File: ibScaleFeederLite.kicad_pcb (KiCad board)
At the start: 4 copper layers, 51.6 x 89 mm, 88 parts, among them J1 PEEL, J2 DRIVE, J3 RAIL, J4 SWD, J5 Serial, SW1 DOWN, SW2 UP, SW3 BOOT, U2 DRV8837, U3 DRV8837, U4 THVD1400D, U5 TPS563300, U6 AMS1117-3.3, U9 STM32F031C6Tx, Y1 8MHz

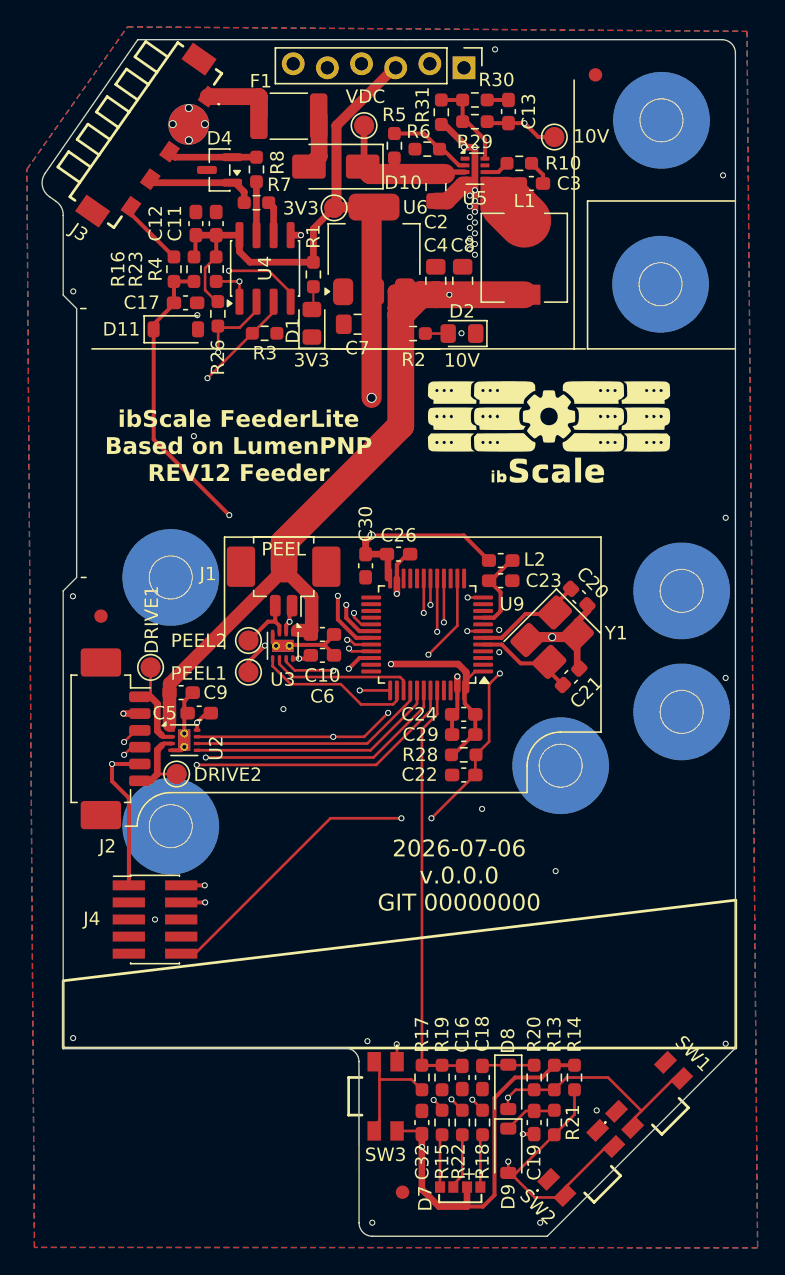
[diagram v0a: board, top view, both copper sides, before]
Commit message: Add labeling to SWD connector
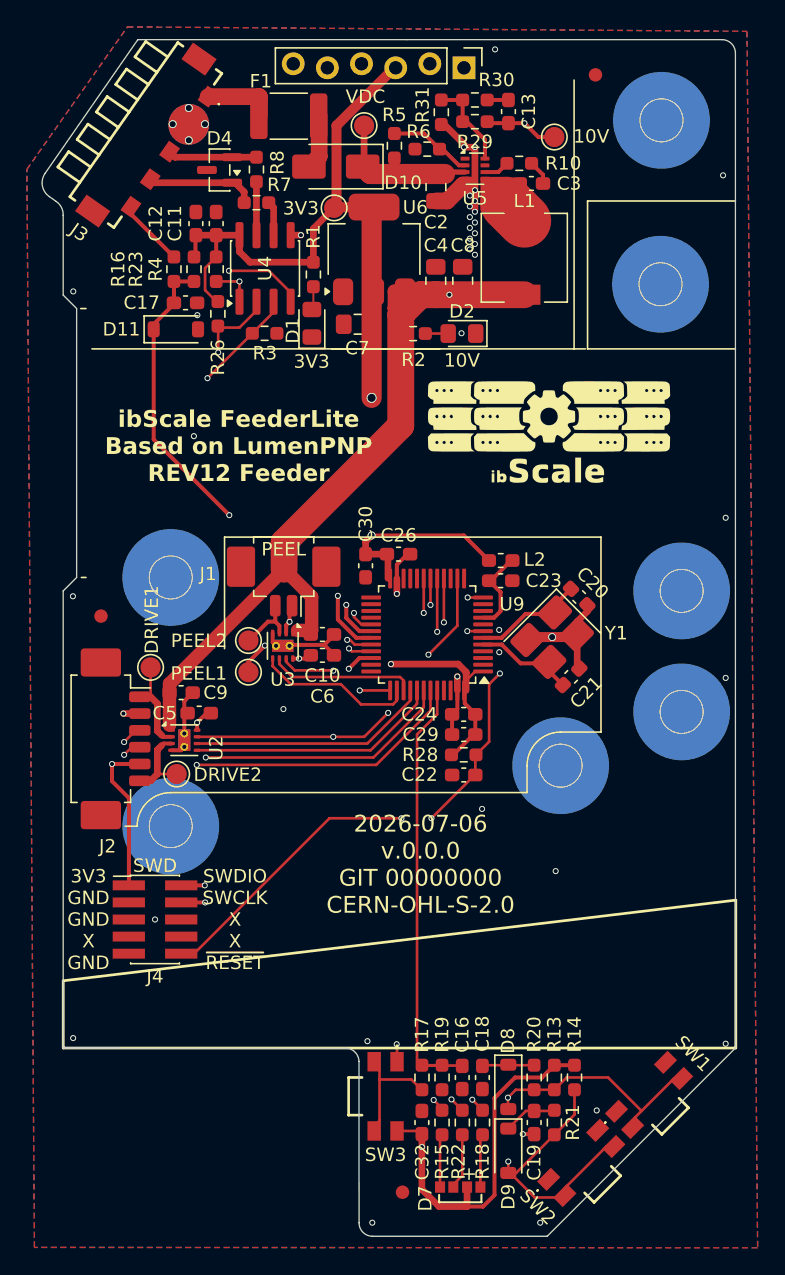
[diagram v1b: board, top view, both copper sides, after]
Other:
- board text added: "2026-07-06 v.0.0.0 GIT 00000000 CERN-OHL-S-2.0"
- board text added: "3V3 GND GND X GND"
- board text added: "SWDIO SWCLK X X ~{RESET}"
- board text removed: "2026-07-06 v.0.0.0 GIT 00000000"
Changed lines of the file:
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@@
 	)
 	(footprint "ibScale:PTCFVTR"
+		(locked yes)
 		(layer "F.Cu")
 		(at 120 104.55 -90)
@@
 	)
 	(footprint "ibScale:PTCFVTR"
+		(locked yes)
 		(layer "F.Cu")
 		(at 134.554594 109.504594 45)
@@
 	)
 	(footprint "ibScale:PTCFVTR"
+		(locked yes)
 		(layer "F.Cu")
 		(at 139.595406 104.445406 45)
@@
 		)
 		(property "Value" "3V3"
-			(at -2.747653 -0.018486 180)
+			(at -2.847653 -0.018486 180)
 			(layer "F.SilkS")
 			(effects
@@
 		(tags "Surface mounted pin header SMD 2x05 1.27mm double row")
 		(property "Reference" "J4"
-			(at -4.7 -0.05 0)
+			(at -0.001274 4.228619 0)
 			(layer "F.SilkS")
 			(effects
@@
 		)
 		(property "Value" "SWD"
-			(at 0 4.285 0)
-			(layer "F.Fab")
+			(at 0.000545 -4.005974 0)
+			(layer "F.SilkS")
 			(effects
 				(font
@@
 		(layer "Edge.Cuts")
 	)
+	(gr_text "3V3\nGND\nGND\nX\nGND"
+		(at 97.9 91.4 0)
+		(layer "F.SilkS")
+		(effects
+			(font
+				(size 1 1)
+				(thickness 0.15)
+			)
+		)
+	)
+	(gr_text "SWDIO\nSWCLK\nX\nX\n~{RESET}"
+		(at 108.8 91.4 0)
+		(layer "F.SilkS")
+		(effects
+			(font
+				(size 1 1)
+				(thickness 0.15)
+			)
+		)
+	)
 	(gr_text "PEEL"
 		(at 112.419869 63.857914 0)
@@
 		)
 	)
-	(gr_text "2026-07-06\nv.0.0.0\nGIT 00000000"
-		(at 125.476 88.138 0)
+	(gr_text "2026-07-06\nv.0.0.0\nGIT 00000000\nCERN-OHL-S-2.0"
+		(at 122.6 87.3 0)
 		(layer "F.SilkS")
 		(effects
@@
 	)
 	(segment
-		(start 122.7066 102.2375)
-		(end 122.7066 77.2634)
+		(start 122.338599 101.869499)
+		(end 122.338599 77.631401)
 		(width 0.2)
 		(layer "F.Cu")
@@
 	)
 	(segment
+		(start 123.8375 76.1325)
+		(end 123.8375 74.3625)
+		(width 0.2)
+		(layer "F.Cu")
+		(net "/BOOT0")
+	)
+	(segment
 		(start 125.61316 102.2625)
 		(end 125.66316 102.3125)
@@
 	)
 	(segment
-		(start 123.8375 76.1325)
-		(end 123.8375 74.3625)
+		(start 122.338599 77.631401)
+		(end 123.8375 76.1325)
 		(width 0.2)
 		(layer "F.Cu")
@@
 	)
 	(segment
-		(start 122.7066 77.2634)
-		(end 123.8375 76.1325)
+		(start 122.7066 102.2375)
+		(end 122.338599 101.869499)
 		(width 0.2)
 		(layer "F.Cu")
@@
 	)
 	(segment
-		(start 107.55 49.225)
-		(end 107.55 47.375)
+		(start 117.35 70.6)
+		(end 117.7 70.95)
 		(width 0.2)
 		(layer "F.Cu")
@@
 	)
 	(segment
-		(start 117.35 70.6)
-		(end 117.7 70.95)
+		(start 117.143955 70.6)
+		(end 117.35 70.6)
 		(width 0.2)
 		(layer "F.Cu")
@@
 	)
 	(segment
-		(start 109.15 47.375)
-		(end 110.4 46.125)
+		(start 107.55 49.225)
+		(end 107.55 47.375)
 		(width 0.2)
 		(layer "F.Cu")
@@
 	)
 	(segment
-		(start 117.143955 70.6)
-		(end 117.35 70.6)
+		(start 107.55 47.375)
+		(end 109.130618 47.375)
 		(width 0.2)
 		(layer "F.Cu")
@@
 	)
 	(segment
-		(start 107.55 47.375)
-		(end 109.15 47.375)
+		(start 117.7 70.95)
+		(end 118.925 70.95)
 		(width 0.2)
 		(layer "F.Cu")
@@
 	)
 	(segment
-		(start 110.4 46.125)
+		(start 110.4 46.105618)
 		(end 110.4 45.44837)
 		(width 0.2)
@@
 	)
 	(segment
-		(start 117.7 70.95)
-		(end 118.925 70.95)
+		(start 109.130618 47.375)
+		(end 110.4 46.105618)
 		(width 0.2)
 		(layer "F.Cu")
@@
 	)
 	(segment
-		(start 115.9 83.87)
-		(end 105.83 93.94)
+		(start 128.5 73.1)
+		(end 127.7 73.9)
 		(width 0.2)
 		(layer "F.Cu")
@@
 	)
 	(segment
-		(start 128.5 73.1)
-		(end 127.7 73.9)
+		(start 115.824347 83.87)
+		(end 105.754347 93.94)
 		(width 0.2)
 		(layer "F.Cu")
@@
 	)
 	(segment
-		(start 105.83 93.94)
-		(end 104.8 93.94)
+		(start 127.7 78.175)
+		(end 126.725 79.15)
 		(width 0.2)
 		(layer "F.Cu")
@@
 	(segment
 		(start 121.18 83.87)
-		(end 115.9 83.87)
+		(end 115.824347 83.87)
 		(width 0.2)
 		(layer "F.Cu")
@@
 	)
 	(segment
-		(start 127.7 78.175)
-		(end 126.725 79.15)
+		(start 127.7 73.9)
+		(end 127.7 78.175)
 		(width 0.2)
 		(layer "F.Cu")
@@
 	)
 	(segment
-		(start 127.7 73.9)
-		(end 127.7 78.175)
+		(start 126.075 69.95)
+		(end 127.25 69.95)
 		(width 0.2)
 		(layer "F.Cu")
@@
 	)
 	(segment
-		(start 126.075 69.95)
-		(end 127.25 69.95)
+		(start 105.754347 93.94)
+		(end 104.8 93.94)
 		(width 0.2)
 		(layer "F.Cu")

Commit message: Have the LDO use solid fille for heat dissipation
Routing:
- net +3.3V: track 210.8 -> 211.7 mm, vias 8 -> 9
- net GND: vias 47 -> 46
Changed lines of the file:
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@@
 			)
 		)
+		(zone_connect 2)
 		(attr smd)
 		(duplicate_pad_numbers_are_jumpers no)
@@
 	)
 	(via
-		(at 126.64375 41.95625)
-		(size 0.45)
-		(drill 0.3)
-		(layers "F.Cu" "B.Cu")
-		(free yes)
-		(net "GND")
-	)
-	(via
 		(at 112.4 75.75)
 		(size 0.45)
@@
 	)
 	(via
+		(at 118.96 51.662556)
+		(size 0.75)
+		(drill 0.6)
+		(layers "F.Cu" "B.Cu")
+		(net "+3.3V")
+	)
+	(via
 		(at 105.979 76.75626)
 		(size 0.45)
@@
 	)
 	(segment
-		(start 118.96 62.835)
-		(end 118.96 52.6)
-		(width 1.5)
-		(layer "In2.Cu")
-		(net "+3.3V")
-	)
-	(segment
 		(start 122.7 102.55)
 		(end 118.96 98.81)
@@
 		(layer "In2.Cu")
 		(net "+3.3V")
+	)
+	(segment
+		(start 118.96 62.835)
+		(end 118.96 51.662556)
+		(width 1.5)
+		(layer "In2.Cu")
+		(net "+3.3V")

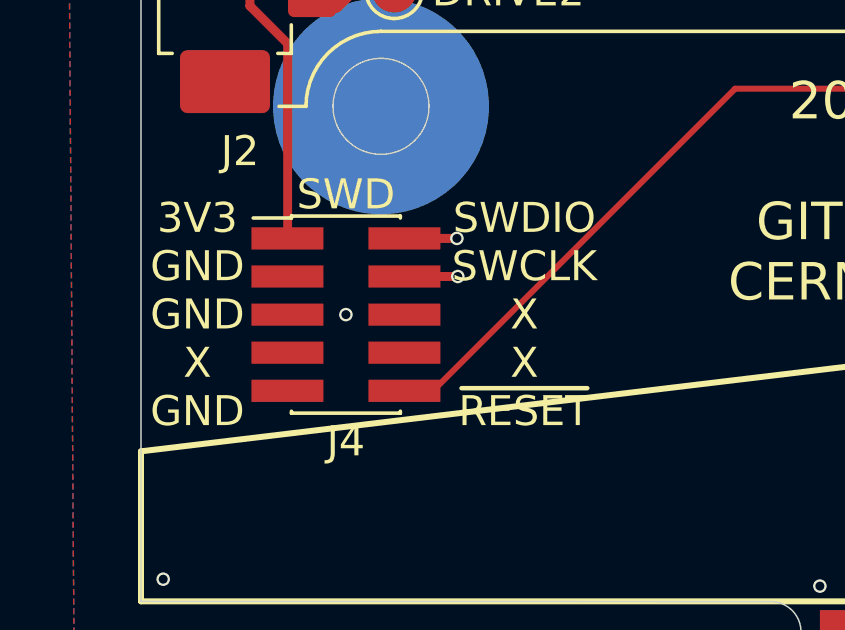
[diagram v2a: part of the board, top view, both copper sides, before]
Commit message: Add SWD header to back of board for in-place debug of a running feeder.
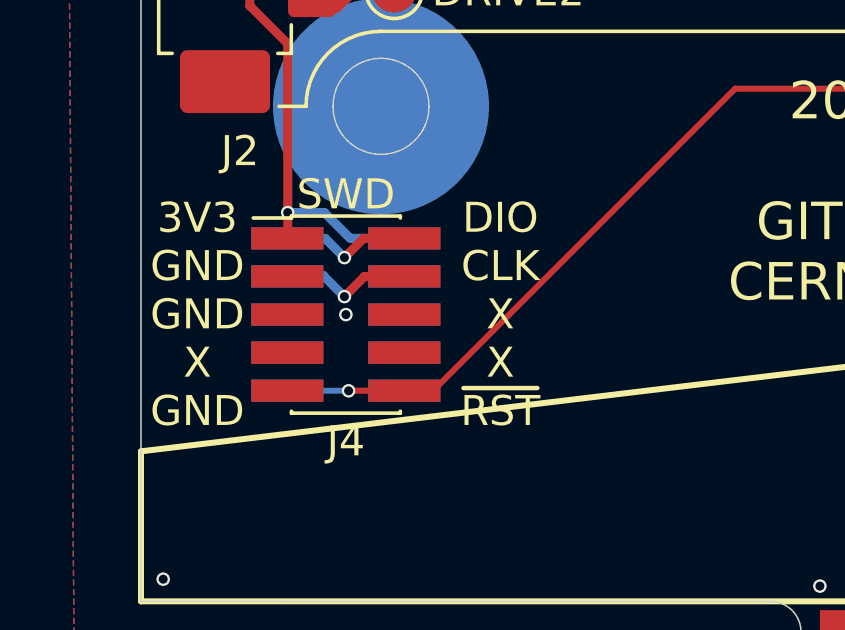
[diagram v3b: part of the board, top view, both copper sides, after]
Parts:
- added J6: SWD, Connector_PinHeader_1.27mm:PinHeader_2x05_P1.27mm_Vertical_SMD, B.Cu at (102.8, 91.4)
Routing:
- net /SWCLK: track 24.6 -> 31.3 mm
- net /SWDIO: track 24.3 -> 31.0 mm
- net +3.3V: track 211.7 -> 216.0 mm, vias 9 -> 10
- net /~{RESET}: track 41.0 -> 44.9 mm, vias 4 -> 5
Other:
- board text added: "DIO CLK X X ~{RST}"
- board text removed: "SWDIO SWCLK X X ~{RESET}"

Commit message: V.1.0 pre-commit
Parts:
- moved TP6 20.5 mm to (121.4, 50.4)
- moved TP8 11.9 mm to (116.1, 50.4)
- moved FID1 7.87 mm to (128.9, 113.5)
- moved R5 2.76 mm to (123.4, 34.2), turned to 180 degrees
- moved TP7 2.71 mm to (120.8, 31.1)
- moved C13 1.67 mm to (130.8, 31.4)
- moved R29 1.67 mm to (128.3, 32.1)
- moved R30 1.67 mm to (128.3, 30.5)
- moved R31 1.67 mm to (125.8, 31.4), turned to -90 degrees
- moved R6 1.38 mm to (123.4, 32.8)
- moved R2 0.38 mm to (122.4, 47.6)
- moved D2 0.38 mm to (126.0, 47.6)
- moved C2 0.38 mm to (124.1, 37.0)
- moved C7 0.18 mm to (118.1, 47.1)
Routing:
- net +10V: track 86.2 -> 71.7 mm
- net +3.3V: track 216.0 -> 226.9 mm, vias 10 -> 11
- net GND: track 41.7 -> 38.4 mm, vias 46 -> 47
- net Net-(U5-EN): track 6.24 -> 3.55 mm
- net VDC: track 11.2 -> 13.5 mm
- net Net-(U5-FB): track 6.82 -> 6.00 mm
- net Net-(J3-Pin_1): track 5.22 -> 4.44 mm
- net /LED_B: track 41.4 -> 42.1 mm
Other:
- board text added: "2026-07-17 v.0.0.1 GIT 00000000 CERN-OHL-S-2.0"
- board text added: "FeederLite 2026-07-17 v.0.0.1 GIT 00000000"
- board text removed: "2026-07-06 v.0.0.0 GIT 00000000 CERN-OHL-S-2.0"
- board text removed: "FeederLite 2026-07-06 v.0.0.0 GIT 00000000"

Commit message: V1.0 ready
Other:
- board text added: "2026-07-17 v.0.0.1 GIT 72fb51ba76 CERN-OHL-S-2.0"
- board text added: "FeederLite 2026-07-17 v.0.0.1 GIT 72fb51ba76"
- board text removed: "2026-07-17 v.0.0.1 GIT 00000000 CERN-OHL-S-2.0"
- board text removed: "FeederLite 2026-07-17 v.0.0.1 GIT 00000000"
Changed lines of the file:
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@@
 		(rev "0.0.1")
 		(company "CERN-OHL-S-2.0")
-		(comment 1 "00000000")
+		(comment 1 "72fb51ba76")
 		(comment 2 "Based on Opulo LumenPNP Rev 12 Feeder mobo")
 		(comment 3 "All 3.3V MLCC ≥16V ±10% ≥X5R; All 10V MLCC ≥25V; All resistors 1% ≥0.1w")
@@
 		)
 	)
-	(gr_text "2026-07-17\nv.0.0.1\nGIT 00000000\nCERN-OHL-S-2.0"
+	(gr_text "2026-07-17\nv.0.0.1\nGIT 72fb51ba76\nCERN-OHL-S-2.0"
 		(at 122.6 87.3 0)
 		(layer "F.SilkS")
@@
 		)
 	)
-	(gr_text "FeederLite\n2026-07-17\nv.0.0.1\nGIT 00000000"
+	(gr_text "FeederLite\n2026-07-17\nv.0.0.1\nGIT 72fb51ba76"
 		(at 108.3564 55.830914 180)
 		(layer "B.SilkS")

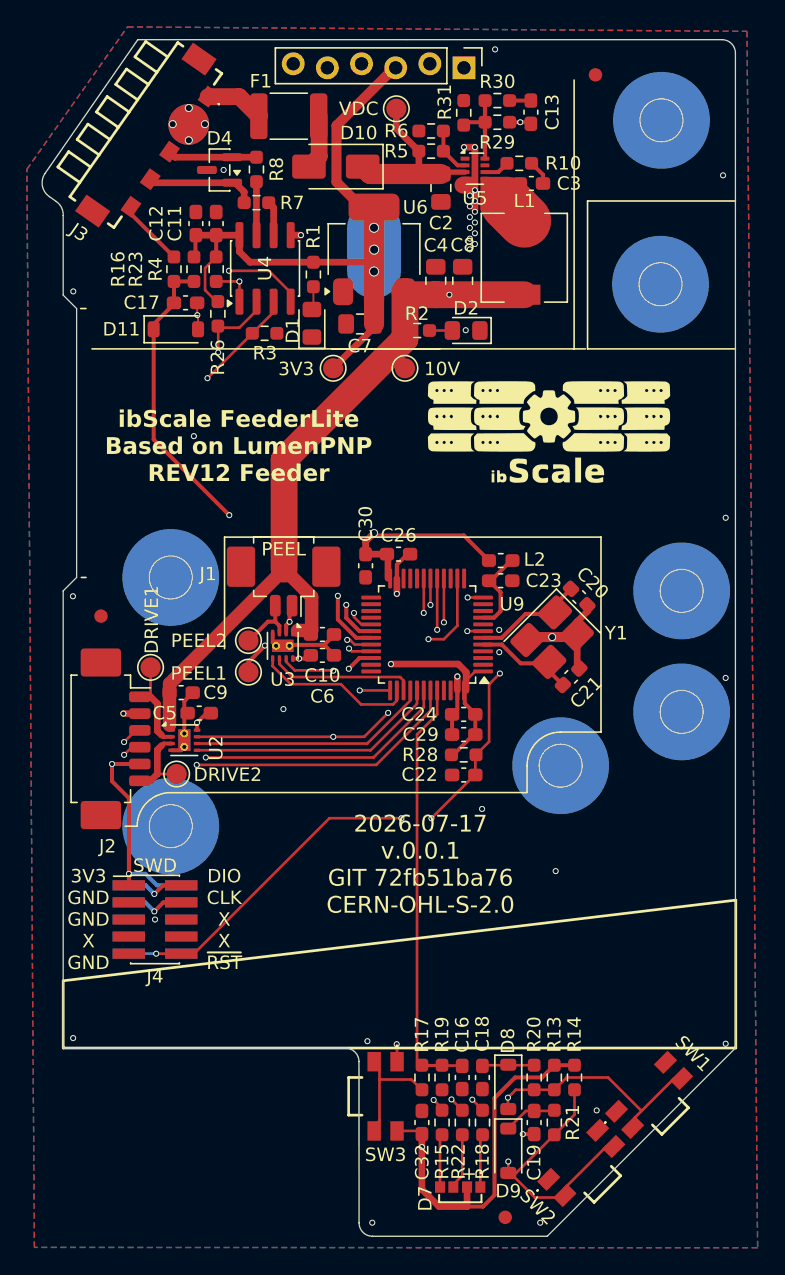
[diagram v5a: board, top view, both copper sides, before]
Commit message: make SWD pinout mirror on both sides
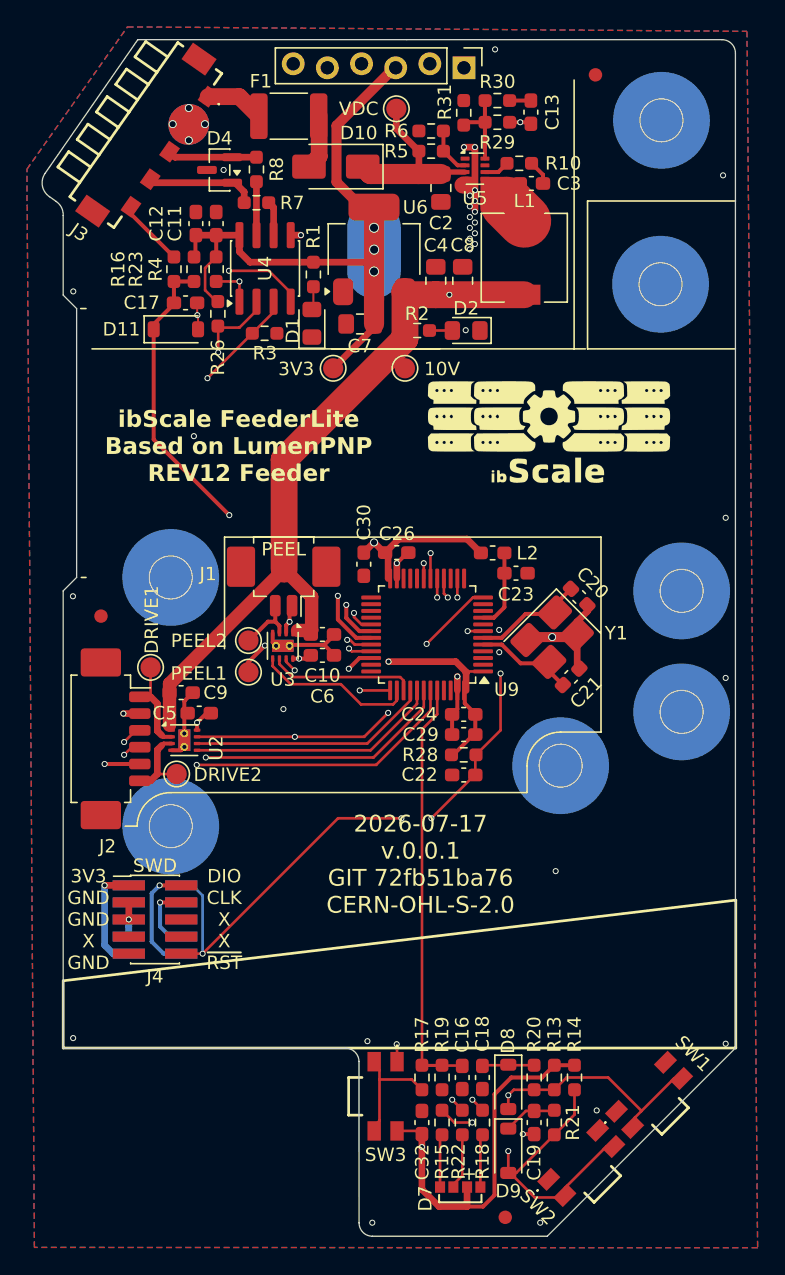
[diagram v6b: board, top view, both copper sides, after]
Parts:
- moved C23 1.27 mm to (129.7, 65.6)
- moved L2 0.83 mm to (128.0, 64.1)
- moved C30 0.18 mm to (118.4, 65.0)
- moved C26 0.18 mm to (120.8, 64.1)
- turned J6 to 0 degrees
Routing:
- net /~{MOTOR_ENABLE}: track 38.1 -> 33.0 mm
- net /SW_DOWN: track 59.5 -> 64.1 mm
- net /SWDIO: track 31.0 -> 34.5 mm
- net /SW_UP: track 66.9 -> 70.1 mm
- net /~{RESET}: track 44.9 -> 47.3 mm
- net /LED_B: track 42.1 -> 44.1 mm
- net GND: track 38.4 -> 39.8 mm, vias 47 -> 46
- net +3.3V: track 226.9 -> 227.7 mm
- net Net-(U9-VDDA): track 6.48 -> 5.95 mm
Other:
- board text added: "GND X GND GND 3V3"
- board text added: "~{RST} X X CLK DIO"

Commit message: Clean up some routing
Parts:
- moved C22 0.21 mm to (125.8, 80.9)
- moved C24 0.21 mm to (125.8, 76.3)
- moved C29 0.21 mm to (125.8, 77.8)
- moved R28 0.21 mm to (125.8, 79.4)
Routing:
- net GND: track 39.8 -> 39.1 mm
